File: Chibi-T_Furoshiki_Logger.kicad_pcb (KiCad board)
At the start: 2 copper layers, 50 x 50 mm, 34 parts, among them J1 M-BUS, J2 from_12V_Power, J3 from_5V_Power, J4 from_ECU_UART, J5 Conn_01x05, U1 MP1584EN-LF-Z, U2 BME280

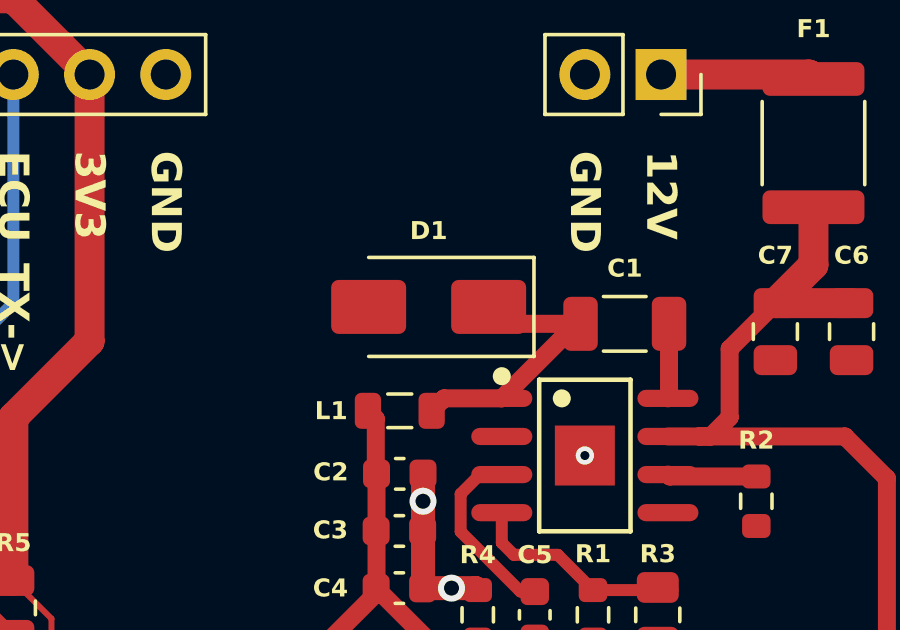
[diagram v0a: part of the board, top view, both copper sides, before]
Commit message: feature: 回路図のバージョンを2.00に更新し、部品L1の情報を追加 BOM、デザインator、ネットリスト、位置情報を新規作成
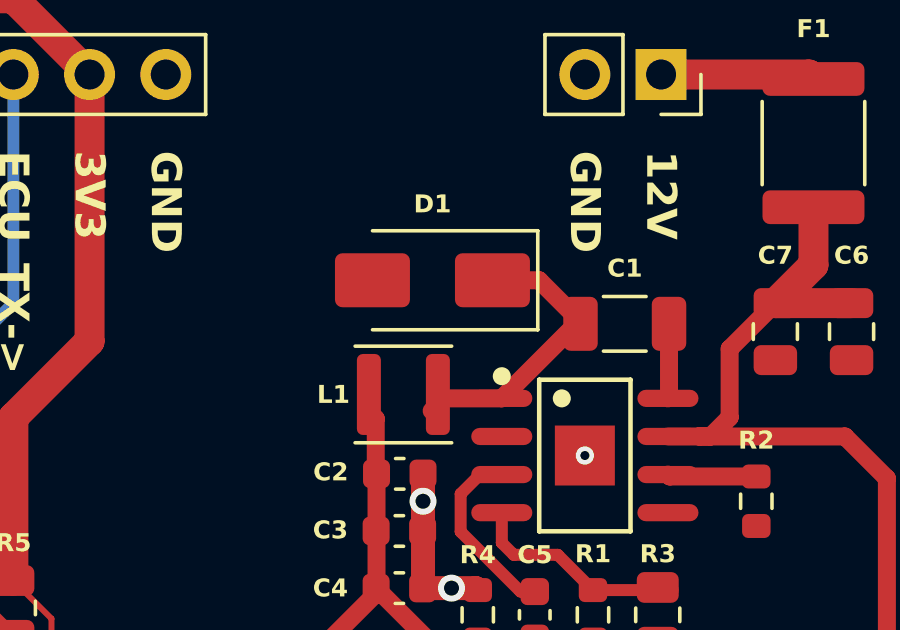
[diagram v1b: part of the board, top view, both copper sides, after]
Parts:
- L1: footprint Inductor_SMD:L_0805_2012Metric -> Inductor_SMD:L_Sunlord_SWPA3015S
- moved D1 0.90 mm to (135.9, 117.3)
- moved L1 0.56 mm to (134.9, 121.2)

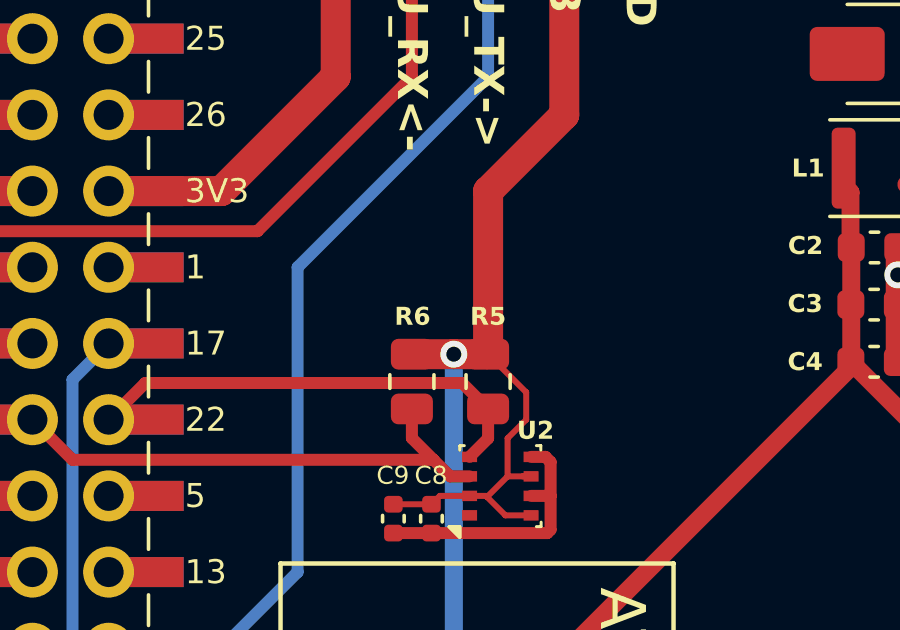
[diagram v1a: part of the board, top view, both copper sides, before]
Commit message: fix: R5およびR6のBOMを修正
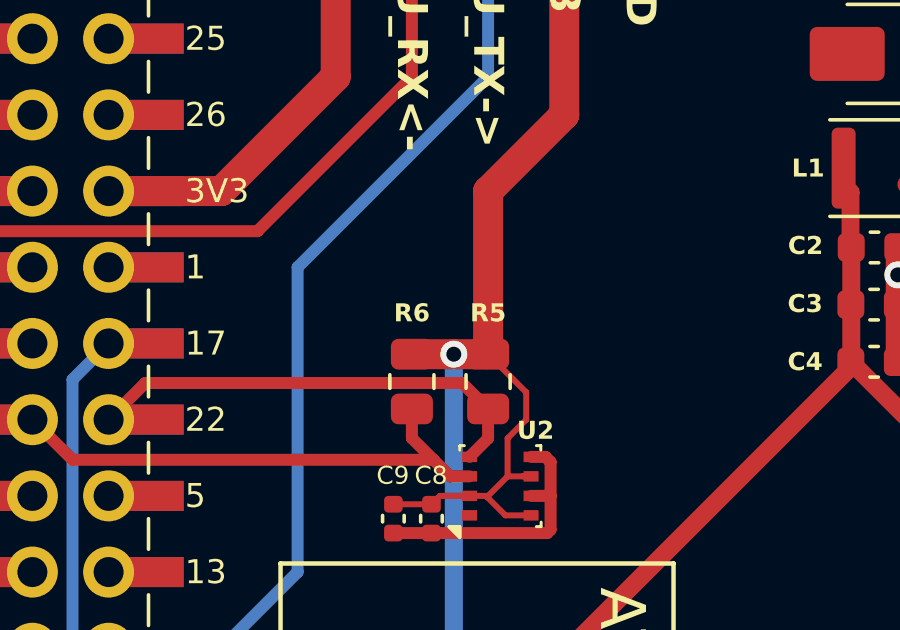
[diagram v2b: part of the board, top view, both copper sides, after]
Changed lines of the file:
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@@
+		)
+	)
+	(footprint "Resistor_SMD:R_0805_2012Metric"
+		(layer "F.Cu")
+		(at 121.92 128.27 -90)
+		(descr "Resistor SMD 0805 (2012 Metric), square (rectangular) end terminal, IPC-7351 nominal, (Body size source: IPC-SM-782 page 72, https://www.pcb-3d.com/wordpress/wp-content/uploads/ipc-sm-782a_amendment_1_and_2.pdf)")
+		(tags "resistor")
+		(property "Reference" "R5"
+			(at -2.286 0 180)
+			(layer "F.SilkS")
+			(effects
+				(font
+					(size 0.6 0.6)
+					(thickness 0.1)
+					(bold yes)
+				)
+			)
+		)
+		(property "Value" "10k"
+			(at 0 1.65 90)
+			(layer "F.Fab")
+			(effects
+				(font
+					(size 1 1)
+					(thickness 0.15)
+				)
+			)
+		)
+		(property "Datasheet" ""
+			(at 0 0 90)
+			(layer "F.Fab")
+			(hide yes)
+			(effects
+				(font
+					(size 1.27 1.27)
+				)
+			)
+		)
+		(property "Description" "Resistor"
+			(at 0 0 90)
+			(layer "F.Fab")
+			(hide yes)
+			(effects
+				(font
+					(size 1.27 1.27)
+				)
+			)
+		)
+		(property "KiLib_Generator" "SMD_2terminal_chip_molded"
+			(at 0 0 90)
+			(layer "F.SilkS")
+			(hide yes)
+			(effects
+				(font
+					(size 1 1)
+					(thickness 0.15)
+				)
+			)
+		)
+		(property "LCSC" "C17414"
+			(at 0 0 270)
+			(unlocked yes)
+			(layer "F.Fab")
+			(hide yes)
+			(effects
+				(font
+					(size 1 1)
+					(thickness 0.15)
+				)
+			)
+		)
+		(property ki_fp_filters "R_*")
+		(sheetname "/")
+		(sheetfile "Chibi-T_Furoshiki_Logger.kicad_sch")
+		(units
+			(unit
+				(name "A")
+				(pins "1" "2")
+			)
+		)
+		(attr smd)
+		(duplicate_pad_numbers_are_jumpers no)
+		(fp_line
+			(start -0.227064 0.735)
+			(end 0.227064 0.735)
+			(stroke
+				(width 0.12)
+				(type solid)
+			)
+			(layer "F.SilkS")
+		)
+		(fp_line
+			(start -0.227064 -0.735)
+			(end 0.227064 -0.735)
+			(stroke
+				(width 0.12)
+				(type solid)
+			)
+			(layer "F.SilkS")
+		)
+		(fp_rect
+			(start -1.68 -0.95)
+			(end 1.68 0.95)
+			(stroke
+				(width 0.05)
+				(type solid)
+			)
+			(fill no)
+			(layer "F.CrtYd")
+		)
+		(fp_rect
+			(start -1 -0.625)
+			(end 1 0.625)
+			(stroke
+				(width 0.1)
+				(type solid)
+			)
+			(fill no)
+			(layer "F.Fab")
+		)
+		(fp_text user "${REFERENCE}"
+			(at 0 0 90)
+			(layer "F.Fab")
+			(effects
+				(font
+					(size 0.5 0.5)
+					(thickness 0.08)
+				)
+			)
+		)
+		(pad "1" smd roundrect
+			(at -0.9125 0 270)
+			(size 1.025 1.4)
+			(layers "F.Cu" "F.Mask" "F.Paste")
+			(roundrect_rratio 0.243902)
+			(net "+3V3")
+			(pintype "passive")
+		)
+		(pad "2" smd roundrect
+			(at 0.9125 0 270)
+			(size 1.025 1.4)
+			(layers "F.Cu" "F.Mask" "F.Paste")
+			(roundrect_rratio 0.243902)
+			(net "SCL")
+			(pintype "passive")
+		)
+		(embedded_fonts no)
+		(model "${KICAD10_3DMODEL_DIR}/Resistor_SMD.3dshapes/R_0805_2012Metric.step"
+			(offset
+				(xyz 0 0 0)
+			)
+			(scale
+				(xyz 1 1 1)
+			)
+			(rotate
+				(xyz 0 0 0)
+			)
 		)
 	)
@@
 		)
 	)
-	(footprint "Resistor_SMD:R_0805_2012Metric"
-		(layer "F.Cu")
-		(at 121.92 128.27 -90)
-		(descr "Resistor SMD 0805 (2012 Metric), square (rectangular) end terminal, IPC-7351 nominal, (Body size source: IPC-SM-782 page 72, https://www.pcb-3d.com/wordpress/wp-content/uploads/ipc-sm-782a_amendment_1_and_2.pdf)")
-		(tags "resistor")
-		(property "Reference" "R5"
-			(at -2.17 0 0)
-			(layer "F.SilkS")
-			(effects
-				(font
-					(size 0.6 0.6)
-					(thickness 0.1)
-					(bold yes)
-				)
-			)
-		)
-		(property "Value" "10k"
-			(at -2.54 0 0)
-			(layer "F.Fab")
-			(effects
-				(font
-					(size 1 1)
-					(thickness 0.15)
-				)
-			)
-		)
-		(property "Datasheet" ""
-			(at 0 0 90)
-			(layer "F.Fab")
-			(hide yes)
-			(effects
-				(font
-					(size 1.27 1.27)
-				)
-			)
-		)
-		(property "Description" "Resistor"
-			(at 0 0 90)
-			(layer "F.Fab")
-			(hide yes)
-			(effects
-				(font
-					(size 1.27 1.27)
-				)
-			)
-		)
-		(property "KiLib_Generator" "SMD_2terminal_chip_molded"
-			(at 0 0 90)
-			(layer "F.SilkS")
-			(hide yes)
-			(effects
-				(font
-					(size 1 1)
-					(thickness 0.15)
-				)
-			)
-		)
-		(property "LCSC" "C17902"
-			(at 0 0 270)
-			(unlocked yes)
-			(layer "F.Fab")
-			(hide yes)
-			(effects
-				(font
-					(size 1 1)
-					(thickness 0.15)
-				)
-			)
-		)
-		(property ki_fp_filters "R_*")
-		(sheetname "/")
-		(sheetfile "Chibi-T_Furoshiki_Logger.kicad_sch")
-		(units
-			(unit
-				(name "A")
-				(pins "1" "2")
-			)
-		)
-		(attr smd)
-		(duplicate_pad_numbers_are_jumpers no)
-		(fp_line
-			(start -0.227064 0.735)
-			(end 0.227064 0.735)
-			(stroke
-				(width 0.12)
-				(type solid)
-			)
-			(layer "F.SilkS")
-		)
-		(fp_line
-			(start -0.227064 -0.735)
-			(end 0.227064 -0.735)
-			(stroke
-				(width 0.12)
-				(type solid)
-			)
-			(layer "F.SilkS")
-		)
-		(fp_rect
-			(start -1.68 -0.95)
-			(end 1.68 0.95)
-			(stroke
-				(width 0.05)
-				(type solid)
-			)
-			(fill no)
-			(layer "F.CrtYd")
-		)
-		(fp_rect
-			(start -1 -0.625)
-			(end 1 0.625)
-			(stroke
-				(width 0.1)
-				(type solid)
-			)
-			(fill no)
-			(layer "F.Fab")
-		)
-		(fp_text user "${REFERENCE}"
-			(at 0 0 0)
-			(layer "F.Fab")
-			(effects
-				(font
-					(size 0.5 0.5)
-					(thickness 0.08)
-				)
-			)
-		)
-		(pad "1" smd roundrect
-			(at -0.9125 0 270)
-			(size 1.025 1.4)
-			(layers "F.Cu" "F.Mask" "F.Paste")
-			(roundrect_rratio 0.243902)
-			(net "+3V3")
-			(pintype "passive")
-		)
-		(pad "2" smd roundrect
-			(at 0.9125 0 270)
-			(size 1.025 1.4)
-			(layers "F.Cu" "F.Mask" "F.Paste")
-			(roundrect_rratio 0.243902)
-			(net "SCL")
-			(pintype "passive")
-		)
-		(embedded_fonts no)
-		(model "${KICAD10_3DMODEL_DIR}/Resistor_SMD.3dshapes/R_0805_2012Metric.step"
-			(offset
-				(xyz 0 0 0)
-			)
-			(scale
-				(xyz 1 1 1)
-			)
-			(rotate
-				(xyz 0 0 0)
-			)
-		)
-	)
 	(footprint "Package_LGA:Bosch_LGA-8_2.5x2.5mm_P0.65mm_ClockwisePinNumbering"
 		(layer "F.Cu")
@@
 	(footprint "Resistor_SMD:R_0805_2012Metric"
 		(layer "F.Cu")
-		(at 119.38 128.27 -90)
+		(at 143.4 128.5 -90)
 		(descr "Resistor SMD 0805 (2012 Metric), square (rectangular) end terminal, IPC-7351 nominal, (Body size source: IPC-SM-782 page 72, https://www.pcb-3d.com/wordpress/wp-content/uploads/ipc-sm-782a_amendment_1_and_2.pdf)")
 		(tags "resistor")
-		(property "Reference" "R6"
-			(at -2.17 -0.02 0)
+		(property "Reference" "R3"
+			(at -2.032 0 180)
 			(layer "F.SilkS")
 			(effects
@@
 		)
 		(property "Value" "10k"
-			(at -2.54 0 0)
+			(at 0 1.65 90)
 			(layer "F.Fab")
 			(effects
@@
 			)
 		)
-		(property "LCSC" "C17902"
+		(property "LCSC" "C17414"
 			(at 0 0 270)
 			(unlocked yes)
@@
 		)
 		(fp_text user "${REFERENCE}"
-			(at 0 0 0)
+			(at 0 0 90)
 			(layer "F.Fab")
 			(effects
@@
 			(layers "F.Cu" "F.Mask" "F.Paste")
 			(roundrect_rratio 0.243902)
-			(net "+3V3")
+			(net "Net-(U1-FB)")
 			(pintype "passive")
 		)
@@
 			(layers "F.Cu" "F.Mask" "F.Paste")
 			(roundrect_rratio 0.243902)
-			(net "SDA")
+			(net "GND")
 			(pintype "passive")
 		)
@@
 	(footprint "Resistor_SMD:R_0805_2012Metric"
 		(layer "F.Cu")
-		(at 143.4 128.5 -90)
+		(at 119.38 128.27 -90)
 		(descr "Resistor SMD 0805 (2012 Metric), square (rectangular) end terminal, IPC-7351 nominal, (Body size source: IPC-SM-782 page 72, https://www.pcb-3d.com/wordpress/wp-content/uploads/ipc-sm-782a_amendment_1_and_2.pdf)")
 		(tags "resistor")
-		(property "Reference" "R3"
-			(at -2.032 0 180)
+		(property "Reference" "R6"
+			(at -2.286 0 180)
 			(layer "F.SilkS")
 			(effects
@@
 			(layers "F.Cu" "F.Mask" "F.Paste")
 			(roundrect_rratio 0.243902)
-			(net "Net-(U1-FB)")
+			(net "+3V3")
 			(pintype "passive")
 		)
@@
 			(layers "F.Cu" "F.Mask" "F.Paste")
 			(roundrect_rratio 0.243902)
-			(net "GND")
+			(net "SDA")
 			(pintype "passive")
 		)
